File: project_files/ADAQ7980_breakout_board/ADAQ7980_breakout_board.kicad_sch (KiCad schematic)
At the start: 14 parts, among them J1 Conn_01x06, J2 Conn_01x06, J3 Conn_01x02

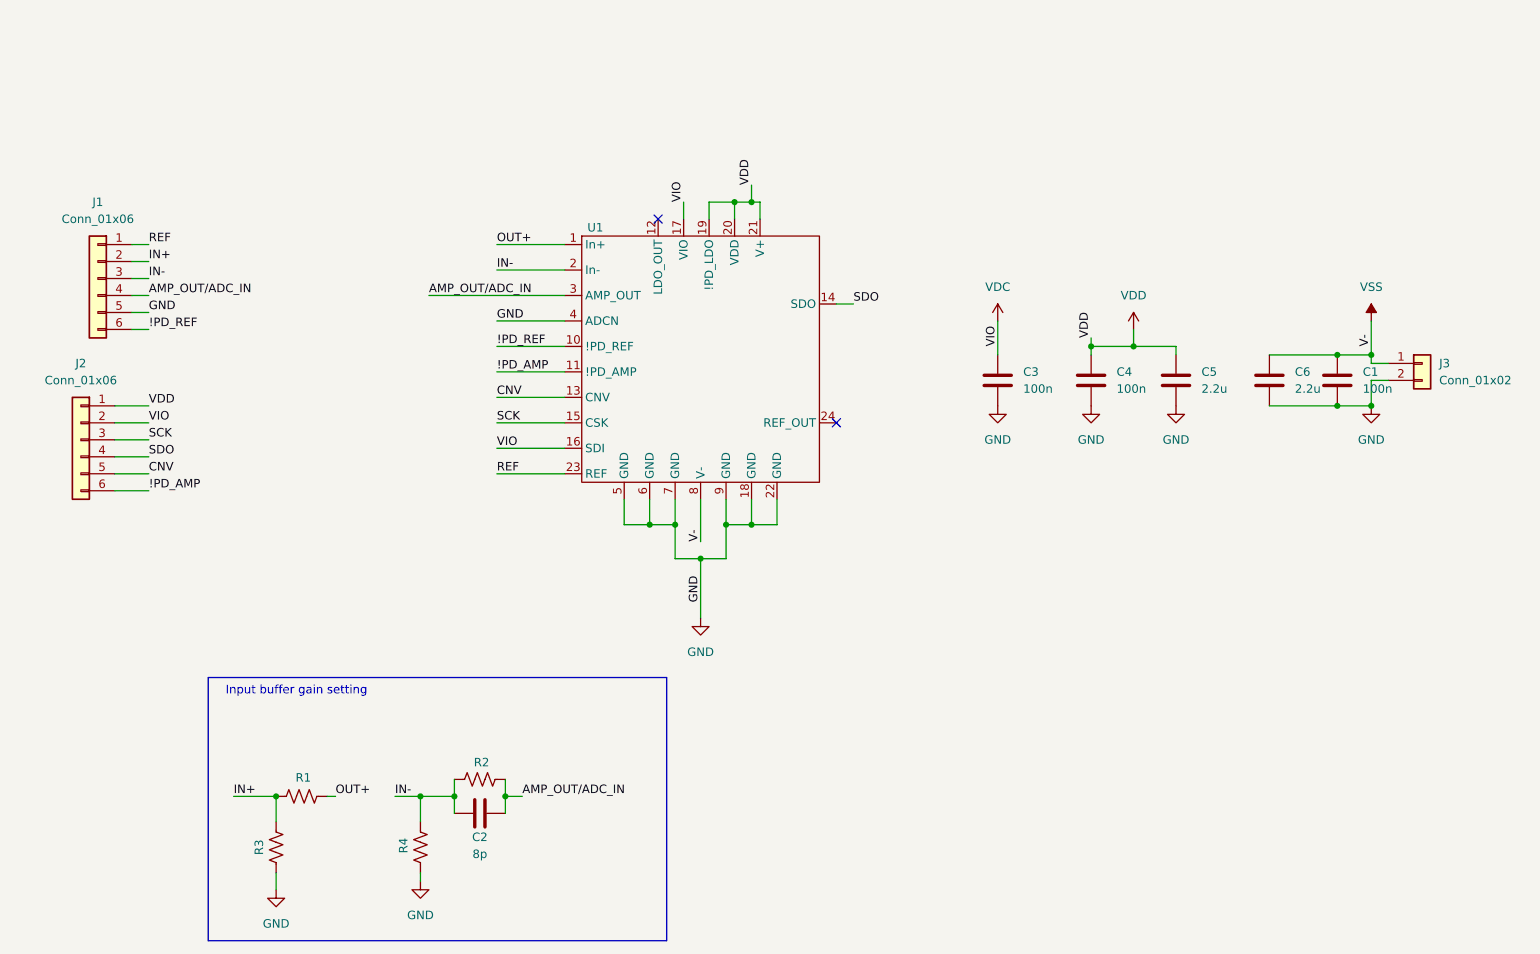
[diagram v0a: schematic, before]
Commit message: -Added precision reference voltage source -Added 47k pull-up resistor for SDO pin -Added SMA-connector for the In+ pin -Added LED power indicator -Extended external pin headers to 8 pins per side -Cleaned up Schematics
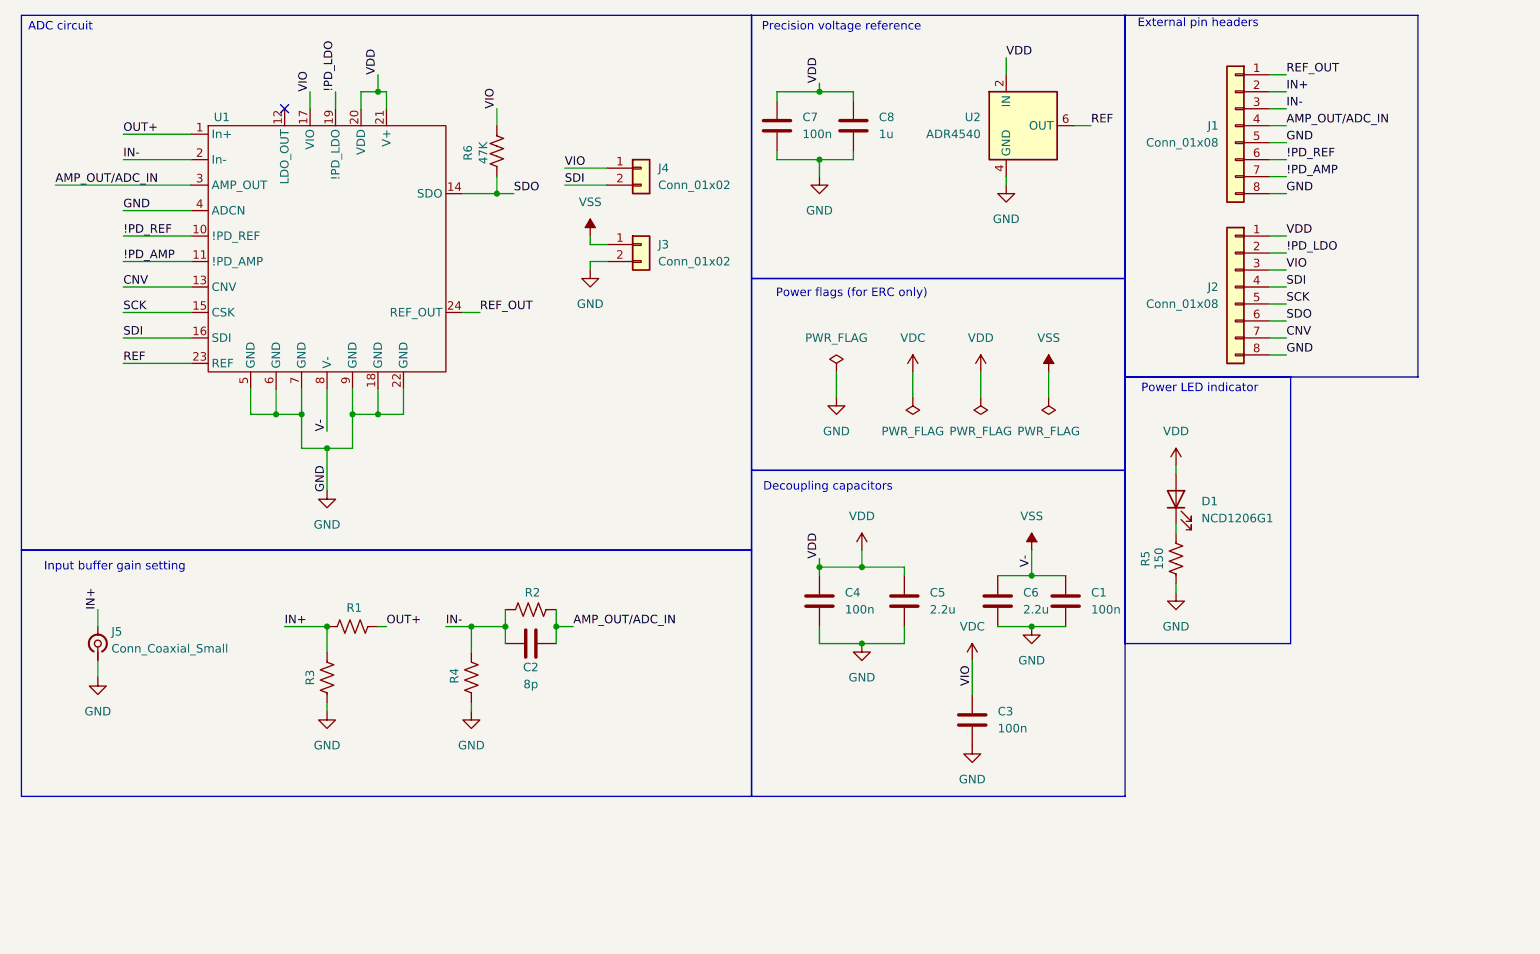
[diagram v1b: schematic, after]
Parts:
- removed J1, J2: Conn_01x06, Connector_PinHeader_2.54mm:PinHeader_1x06_P2.54mm_Vertical, symbol ADAQ7980_breakout:Conn_01x06
- added C7: 100n, ADAQ_breakout:C_0603_1608Metric, symbol ADAQ_breakout:C
- added C8: 1u, ADAQ_breakout:C_0603_1608Metric, symbol ADAQ_breakout:C
- added D1: NCD1206G1, LED_SMD:LED_1206_3216Metric, symbol ADAQ_breakout:NCD1206G1
- added J1, J2: Conn_01x08, Connector_PinSocket_2.54mm:PinSocket_1x08_P2.54mm_Vertical, symbol ADAQ_breakout:Conn_01x08
- added J4: Conn_01x02, Connector_PinHeader_2.54mm:PinHeader_1x02_P2.54mm_Vertical, symbol ADAQ_breakout:Conn_01x02
- added J5: Conn_Coaxial_Small, ADAQ_breakout:SMA_Amphenol_132134-11_Vertical, symbol ADAQ_breakout:Conn_Coaxial_Small
- added R5: 150, ADAQ_breakout:R_0603_1608Metric, symbol ADAQ_breakout:R_US
- added R6: 47K, ADAQ_breakout:R_0603_1608Metric, symbol ADAQ_breakout:R_US
- added U2: ADR4540, Package_SO:SOIC-8_3.9x4.9mm_P1.27mm, symbol ADAQ_breakout:ADR4540
- C1, C2, C3, C4, C5, C6: symbol ADAQ7980_breakout:C -> ADAQ_breakout:C
- J3: symbol ADAQ7980_breakout:Conn_01x02 -> ADAQ_breakout:Conn_01x02
- R1, R2, R3, R4: value (none) -> 49.9; symbol ADAQ7980_breakout:R_US -> ADAQ_breakout:R_US
- U1: symbol ADAQ7980_breakout:ADAQ7980BCCZ -> ADAQ_breakout:ADAQ7980BCCZ
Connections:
- net !PD_AMP: now also J1.7 (Pin_7)
- net !PD_REF: now also J1.6 (Pin_6)
- net AMP_OUT/ADC_IN: now also J1.4 (Pin_4)
- net CNV: now also J2.7 (Pin_7)
- net GND: now also C7.2, C8.2, J1.5 (Pin_5), J1.8 (Pin_8), J2.8 (Pin_8), J5.1 (In), R5.1, U2.4 (GND)
- net IN+: now also J1.2 (Pin_2), J5.2 (Ext)
- net IN-: now also J1.3 (Pin_3)
- net REF: now also U2.6 (OUT)
- net SCK: now also J2.5 (Pin_5)
- net SDO: now also J2.6 (Pin_6), R6.1
- net VDC: now also J2.3 (Pin_3), J4.1 (Pin_1), R6.2; no longer U1.16 (SDI)
- net VDD: now also C7.1, C8.1, D1.2 (A), J2.1 (Pin_1), U2.2 (IN); no longer U1.19 (!PD_LDO)
- net REF_OUT: now reaches U1.24 (REF_OUT)
- net REF_OUT: now also J1.1 (Pin_1)
- new net: D1.1 (K), R5.2
- new net !PD_LDO: J2.2 (Pin_2), U1.19 (!PD_LDO)
- new net SDI: J2.4 (Pin_4), J4.2 (Pin_2), U1.16 (SDI)
- no-connect marks 2 -> 1
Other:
- note added: "ADC circuit"
- note added: "Decoupling capacitors"
- note added: "External pin headers"
- note added: "Power LED indicator"
- note added: "Power flags (for ERC only)"
- note added: "Precision voltage reference"
- moved on the sheet: C1, C2, C3, C4, C5, C6, J3, R1, R2, R3, R4, U1
